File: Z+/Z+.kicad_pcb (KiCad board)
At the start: 4 copper layers, 98 x 98 mm, 159 parts, among them J1 200528-0100, Q1 NX3008NBKS, Q10 NX3008NBKS, Q11 MBT2222ADW1T1, Q12 MBT2222ADW1T1, Q13 NX3008NBKS, Q14 NX3008NBKS, Q15 MBT2222ADW1T1, Q16 MBT2222ADW1T1, Q2 NX3008NBKS, Q3 MBT2222ADW1T1, Q4 MBT2222ADW1T1, Q5 NX3008NBKS, Q6 NX3008NBKS, Q7 MBT2222ADW1T1, Q8 MBT2222ADW1T1, Q9 NX3008NBKS, U1 SI3865DDV-T1-GE3, U2 LTC4376CDHD_PBF, U4 ADM1176-1ARMZ-R7, U5 ADM1176-1ARMZ-R7, U6 NCV891330PD50R2G, U7 DRV8830DRC, U8 LTC3130, U9 SunSensor

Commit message: Z+ updates WIP
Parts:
- removed C34, C35: 0.1uF, Capacitor_SMD:C_0402_1005Metric
- removed FL1: SRF2012, SolarPanels:SRF2012
- removed L2: 6.8uH, Inductor_SMD:L_Coilcraft_LPS4018
- removed Ref**: Val**, custom-footprints:ypanel
- added D10: DFLS130L-7, Diode_SMD:D_PowerDI-123, B.Cu at (18.9, 74.8)
- added F1: Fuse_Small, Fuse:Fuse_0603_1608Metric, B.Cu at (-19.4, 101.4)
- added F2: Fuse_Small, Fuse:Fuse_0603_1608Metric, B.Cu at (-19.4, 103.9)
- added F3: Fuse_Small, Fuse:Fuse_0603_1608Metric, B.Cu at (-19.4, 106.5)
- added F4: Fuse_Small, Fuse:Fuse_0603_1608Metric, B.Cu at (-19.4, 109.0)
- added F5: 500mA, Fuse:Fuse_0603_1608Metric, B.Cu at (80.9, 117.2)
- added F6: 500mA, Fuse:Fuse_0603_1608Metric, B.Cu at (17.9, 87.4)
- added F7: 100mA, Fuse:Fuse_0603_1608Metric, B.Cu at (24.0, 58.5)
- added Q17: MBT2222ADW1T1, Package_TO_SOT_SMD:SOT-363_SC-70-6, B.Cu at (46.8, 56.7)
- added Q18: NX3008NBKS, Package_TO_SOT_SMD:SOT-363_SC-70-6, B.Cu at (46.8, 60.6)
- added Q19: MBT2222ADW1T1, Package_TO_SOT_SMD:SOT-363_SC-70-6, B.Cu at (57.1, 56.7)
- added Q20: NX3008NBKS, Package_TO_SOT_SMD:SOT-363_SC-70-6, B.Cu at (67.3, 76.3)
- added Q21: MBT2222ADW1T1, Package_TO_SOT_SMD:SOT-363_SC-70-6, B.Cu at (57.1, 95.8)
- added Q22: NX3008NBKS, Package_TO_SOT_SMD:SOT-363_SC-70-6, B.Cu at (57.1, 99.8)
- added Q23: MBT2222ADW1T1, Package_TO_SOT_SMD:SOT-363_SC-70-6, B.Cu at (57.1, 103.7)
- added Q24: NX3008NBKS, Package_TO_SOT_SMD:SOT-363_SC-70-6, B.Cu at (77.6, 56.7)
- added Q25: MBT2222ADW1T1, Package_TO_SOT_SMD:SOT-363_SC-70-6, B.Cu at (77.6, 60.6)
- added Q26: NX3008NBKS, Package_TO_SOT_SMD:SOT-363_SC-70-6, B.Cu at (46.8, 76.3)
- added Q27: MBT2222ADW1T1, Package_TO_SOT_SMD:SOT-363_SC-70-6, B.Cu at (46.8, 80.2)
- added R100: DNI (0R), Resistor_SMD:R_0603_1608Metric, B.Cu at (63.2, 63.5)
- added R101: 10K, Resistor_SMD:R_0603_1608Metric, B.Cu at (63.2, 66.0)
- added R102: 10K, Resistor_SMD:R_0603_1608Metric, B.Cu at (63.2, 68.5)
- added R103: 200K, Resistor_SMD:R_0603_1608Metric, B.Cu at (63.2, 71.0)
- added R64: DNI (0R), Resistor_SMD:R_0603_1608Metric, B.Cu at (42.7, 63.5)
- added R65: 10K, Resistor_SMD:R_0603_1608Metric, B.Cu at (42.7, 66.0)
- added R75: 100K, Resistor_SMD:R_0603_1608Metric, B.Cu at (63.2, 80.5)
- added R76: DNI (0R), Resistor_SMD:R_0603_1608Metric, B.Cu at (63.2, 83.0)
- added R77: 10K, Resistor_SMD:R_0603_1608Metric, B.Cu at (63.2, 85.6)
- added R78: 10K, Resistor_SMD:R_0603_1608Metric, B.Cu at (63.2, 88.1)
- added R79: 200K, Resistor_SMD:R_0603_1608Metric, B.Cu at (63.2, 90.6)
- added R80: 680R, Resistor_SMD:R_0603_1608Metric, B.Cu at (52.9, 97.6)
- added R81: 100K, Resistor_SMD:R_0603_1608Metric, B.Cu at (52.9, 100.1)
- added R82: DNI (0R), Resistor_SMD:R_0603_1608Metric, B.Cu at (52.9, 102.6)
- added R83: 10K, Resistor_SMD:R_0603_1608Metric, B.Cu at (52.9, 105.1)
- added R84: 10K, Resistor_SMD:R_0603_1608Metric, B.Cu at (52.9, 107.6)
- added R85: 200K, Resistor_SMD:R_0603_1608Metric, B.Cu at (52.9, 110.1)
- added R86: 680R, Resistor_SMD:R_0603_1608Metric, B.Cu at (73.5, 58.5)
- added R87: 100K, Resistor_SMD:R_0603_1608Metric, B.Cu at (73.5, 61.0)
- added R88: DNI (0R), Resistor_SMD:R_0603_1608Metric, B.Cu at (73.5, 63.5)
- added R89: 10K, Resistor_SMD:R_0603_1608Metric, B.Cu at (73.5, 66.0)
- added R90: 10K, Resistor_SMD:R_0603_1608Metric, B.Cu at (73.5, 68.5)
- added R91: 200K, Resistor_SMD:R_0603_1608Metric, B.Cu at (73.5, 71.0)
- added R92: 680R, Resistor_SMD:R_0603_1608Metric, B.Cu at (42.7, 78.0)
- added R93: 100K, Resistor_SMD:R_0603_1608Metric, B.Cu at (42.7, 80.5)
- added R94: DNI (0R), Resistor_SMD:R_0603_1608Metric, B.Cu at (42.7, 83.0)
- added R95: 10K, Resistor_SMD:R_0603_1608Metric, B.Cu at (42.7, 85.6)
- added R96: 10K, Resistor_SMD:R_0603_1608Metric, B.Cu at (42.7, 88.1)
- added R97: 200K, Resistor_SMD:R_0603_1608Metric, B.Cu at (42.7, 90.6)
- added R98: 680R, Resistor_SMD:R_0603_1608Metric, B.Cu at (63.2, 58.5)
- added R99: 100K, Resistor_SMD:R_0603_1608Metric, B.Cu at (63.2, 61.0)
- added U3: SunSensor, Argus-IC:SunSensor, F.Cu at (103.5, 101.9)
- C1, C2, C5, C6, C7, C8: value 10nF -> 100nF
- C10: value 1nF -> 0.1uF
- C11: value 1uF -> 10uF; footprint Capacitor_SMD:C_1206_3216Metric -> Capacitor_SMD:C_1210_3225Metric
- C12: footprint Capacitor_SMD:C_0402_1005Metric -> Capacitor_SMD:C_0603_1608Metric; moved to B.Cu
- C13: value 3.3nF -> 1nF
- C14: value 3.3nF -> 0.1uF
- C15: value 4.7uF -> 10nF; footprint Capacitor_SMD:C_1210_3225Metric -> Capacitor_SMD:C_0603_1608Metric
- C16: value 0.1uF -> 10nF; footprint Capacitor_SMD:C_0805_2012Metric -> Capacitor_SMD:C_0603_1608Metric
- C17: value 1uF -> 3.3nF; footprint Capacitor_SMD:C_0805_2012Metric -> Capacitor_SMD:C_0603_1608Metric
- C18: value 0.1uF -> 47uF; footprint Capacitor_SMD:C_0603_1608Metric -> Capacitor_SMD:C_1210_3225Metric
- C19: value 0.1uF -> 10uF; footprint Capacitor_SMD:C_0603_1608Metric -> Capacitor_SMD:C_1210_3225Metric
- C20: value 0.1uF -> 1uF; footprint Capacitor_SMD:C_0603_1608Metric -> Capacitor_SMD:C_0805_2012Metric
- C21: value 10uF -> 1uF; footprint Capacitor_SMD:C_1206_3216Metric -> Capacitor_SMD:C_0805_2012Metric
- C22, C23: value 10uF -> 22nF; footprint Capacitor_SMD:C_1206_3216Metric -> Capacitor_SMD:C_0603_1608Metric
- C24: value 47uF -> 4.7uF; footprint Capacitor_SMD:C_1210_3225Metric -> Capacitor_SMD:C_0603_1608Metric
- C25: value 10uF -> 1uF; footprint Capacitor_SMD:C_1210_3225Metric -> Capacitor_SMD:C_0805_2012Metric
- C26: value 1uF -> 47uF; footprint Capacitor_SMD:C_0805_2012Metric -> Capacitor_SMD:C_1210_3225Metric
- C27, C31: value 1uF -> 10nF; footprint Capacitor_SMD:C_0805_2012Metric -> Capacitor_SMD:C_0603_1608Metric
- C28, C29: value 22nF -> 10nF
- C30: value 4.7uF -> 10nF
- C32: value 47uF -> 10nF; footprint Capacitor_SMD:C_1210_3225Metric -> Capacitor_SMD:C_0603_1608Metric
- C33: value 0.1uF -> 10nF; footprint Capacitor_SMD:C_0402_1005Metric -> Capacitor_SMD:C_0603_1608Metric; moved to B.Cu
- C9: value 10uF -> 10nF; footprint Capacitor_SMD:C_1206_3216Metric -> Capacitor_SMD:C_0603_1608Metric
- D1: value DFLS130L-7 -> ESD5Zxx; footprint Diode_SMD:D_PowerDI-123 -> Diode_SMD:D_SOD-523; moved to B.Cu
- D2: value DFLS130L-7 -> PMEG4005EH; footprint Diode_SMD:D_PowerDI-123 -> Diode_SMD:D_SOD-123F; moved to B.Cu
- D3: value DFLS130L-7 -> GREEN; footprint Diode_SMD:D_PowerDI-123 -> LED_SMD:LED_0603_1608Metric; moved to B.Cu
- D4: value DFLS130L-7 -> 10V; footprint Diode_SMD:D_PowerDI-123 -> Diode_SMD:Nexperia_DSN1608-2_1.6x0.8mm; moved to B.Cu
- D5, D6: moved to B.Cu
- D7: value BAS16HT1G -> DFLS130L-7; footprint Diode_SMD:D_SOD-323 -> Diode_SMD:D_PowerDI-123
- D8: value NRVB440MFS -> DFLS130L-7; footprint SolarPanels:NRVB440MFSWFT1G -> Diode_SMD:D_PowerDI-123
- D9: value LSM115 -> DFLS130L-7; footprint SolarPanels:DO-214BA_MCH -> Diode_SMD:D_PowerDI-123
- H1, H2, H3, H4, H5, H6, H7, H8: footprint SolarPanels:MountingHole_3.2mm_M3_DIN965_Pad_TopBottom -> Argus-Miscellaneous:MountingHole_3.2mm_M3_DIN965_Pad_TopBottom
- J1: footprint Connector_FFC-FPC:Molex_200528-0100_1x10-1MP_P1.00mm_Horizontal -> Argus-Connectors:Molex_200528-0100_1x10-1MP_P1.00mm_Horizontal
- L1: value XGL3520-222 -> 6.8uH; footprint SolarPanels:XGL3520 -> Argus-Passives:L_Coilcraft_LPS4018
- Q12, Q16, Q3: value MBT2222ADW1T1 -> NX3008NBKS
- Q13, Q2, Q6: value NX3008NBKS -> MBT2222ADW1T1
- Q7: value MBT2222ADW1T1 -> SiRA99DP; footprint Package_TO_SOT_SMD:SOT-363_SC-70-6 -> Argus-Miscellaneous:PowerPAK SO-8
- Q8: value MBT2222ADW1T1 -> IRLML2803; footprint Package_TO_SOT_SMD:SOT-363_SC-70-6 -> Package_TO_SOT_SMD:SOT-23
- Q9: value NX3008NBKS -> SiRA99DP; footprint Package_TO_SOT_SMD:SOT-363_SC-70-6 -> Argus-Miscellaneous:PowerPAK SO-8
- R1, R68, R74: value 0R -> 680R
- R10, R11: value 680R -> 10K
- R12: value 100K -> 200K
- R13, R7: value 100K -> 680R
- R14: value DNI (0R) -> 100K
- R18, R41, R54: value 10K -> 200K
- R19: value 200K -> 2.7k
- R2: value 0R -> 100K
- R20, R28, R29, R30, R59: value 10K -> 0R
- R21, R31, R57: value 200K -> 0R
- R22: value 680R -> 10k
- R23: value 680R -> 4k7
- R24: value DNI (0R) -> 10k
- R25: value DNI (0R) -> 0R
- R26: value 100K -> 0R
- R27: value 100K -> 10k
- R3, R70: value 0R -> DNI (0R)
- R32: value 10K -> TBD
- R33: value 200K -> 1k
- R34, R35: value DNI (0R) -> TBD
- R37: value 680R -> 100K
- R38: value 100K -> DNI (0R)
- R39: value 100K -> 10K
- R4, R66, R72: value 0R -> 10K
- R42: value 10K -> 680R
- R43: value 200K -> 100K
- R44: value 10K -> DNI (0R)
- R45: value 200K -> 10K
- R46: value DNI (0R) -> 10K
- R47: value DNI (0R) -> 200K
- R48, R49: value 680R -> 1.91M
- R5: value R_Small -> 10K
- R50: value 100K -> 126k
- R51: value 100K -> 182k
- R52, R69: value 10K -> 100K
- R53: value 10K -> 1.47M
- R55: value 200K -> ?R; footprint Resistor_SMD:R_0603_1608Metric -> Resistor_SMD:R_2512_6332Metric
- R56: value 10K -> 1K
- R58: value 100K -> 0R (DNI)
- R6: value R_Small -> 200K
- R60, R61: value ?R -> 0R; footprint Resistor_SMD:R_2512_6332Metric -> Resistor_SMD:R_0603_1608Metric
- R62: value 1K -> 680R
- R63: value 1K -> 100K
- R67, R73: value 0R -> 200K
- R71: value 0R (DNI) -> 10K
- R8: value R_Small -> 100K
- R9: value R_Small -> DNI (0R)
- SC1, SC2, SC3, SC4, SC5, SC6: value SM141K06TF -> SM141K06L; footprint SolarPanels:SM141K06TF -> Argus-Miscellaneous:SM141K06TF
- U1: value SI3865DDV-T1-GE3 -> USBLC6-2P6; footprint Package_TO_SOT_SMD:SOT-23-6 -> Package_TO_SOT_SMD:SOT-666
- U2: value LTC4376CDHD_PBF -> SunSensor; footprint Package_DFN_QFN:DFN-16-1EP_4x5mm_P0.5mm_EP2.44x4.34mm -> Argus-IC:SunSensor
- U4, U5: value ADM1176-1ARMZ-R7 -> SunSensor; footprint Package_SO:MSOP-10_3x3mm_P0.5mm -> Argus-IC:SunSensor
- U6: value NCV891330PD50R2G -> LTC4412xS6; footprint Package_SO:SOIC-8-1EP_3.9x4.9mm_P1.27mm_EP2.514x3.2mm -> Package_TO_SOT_SMD:TSOT-23-6
- U7: value DRV8830DRC -> DRV8235RTER; footprint Package_SON:VSON-10-1EP_3x3mm_P0.5mm_EP1.65x2.4mm -> Argus-IC:WQFN16_RTE_TEX
- U8: value LTC3130 -> ADM1176-1ARMZ-R7; footprint Package_DFN_QFN:QFN-20-1EP_3x4mm_P0.5mm_EP1.65x2.65mm -> Package_SO:MSOP-10_3x3mm_P0.5mm
- U9: value SunSensor -> LTC3130; footprint SolarPanels:SunSensor -> Package_DFN_QFN:QFN-20-1EP_3x4mm_P0.5mm_EP1.65x2.65mm; moved to B.Cu
- moved C7 183.6 mm to (-19.4, 96.4), turned to 180 degrees
- moved U2 182.3 mm to (-8.12, 92.1), turned to 180 degrees
- moved U4 179.0 mm to (-8.12, 100.1)
- moved D3 177.8 mm to (18.0, 97.5), turned to 180 degrees
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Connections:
- C1 pad 1: Net-(Q1B-G1) -> MAIN_3V3
- C10 pad 1: Net-(U1-R1,C1) -> Net-(D2-A)
- C10 pad 2: Net-(D9-A) -> GND
- C11 pad 1: Net-(D9-A) -> /Coil Driver/VM
- C12 pad 1: 3.3V -> /Coil Driver/VM
- C13 pad 1: GND -> /Coil Driver/IPROPI
- C13 pad 2: Net-(U4-TIMER) -> GND
- C14 pad 1: GND -> /Coil Driver/VREF
- C14 pad 2: Net-(U5-TIMER) -> GND
- C15 pad 1: GND -> Net-(Q10B-G1)
- C15 pad 2: VDRIVE -> GND
- C16 pad 1: +5V -> Net-(Q12B-G1)
- C17 pad 2: VDRIVE -> Net-(U8-TIMER)
- C18 pad 1: GND -> /Solar Charger/MPPT2/VIN
- C18 pad 2: Net-(D7-A) -> GND
- C19 pad 1: Net-(D7-K) -> /Solar Charger/MPPT2/VIN
- C19 pad 2: Net-(D8-K) -> GND
- C2 pad 1: Net-(Q2B-G1) -> PERI_3V3
- C20 pad 1: GND -> /Solar Charger/MPPT2/VIN
- C20 pad 2: +5V -> GND
- C21 pad 1: GND -> /Solar Charger/MPPT2/VIN
- C21 pad 2: +5V -> GND
- C22 pad 1: GND -> Net-(U9-SW1)
- C22 pad 2: +5V -> Net-(U9-BST1)
- C23 pad 1: GND -> Net-(U9-BST2)
- C23 pad 2: +5V -> Net-(U9-SW2)
- C24 pad 1: VSOLAR -> /Solar Charger/MPPT2/VCC
- C25 pad 1: VSOLAR -> /Solar Charger/Charge OR-ing2/IN
- C26 pad 1: VSOLAR -> /Solar Charger/Charge OR-ing2/IN
- C27 pad 1: VSOLAR -> Net-(Q14B-G1)
- C28 pad 1: Net-(U8-SW1) -> Net-(Q16B-G1)
- C28 pad 2: Net-(U8-BST1) -> GND
- C29 pad 1: Net-(U8-BST2) -> Net-(Q18B-G1)
- C29 pad 2: Net-(U8-SW2) -> GND
- C3 pad 1: Net-(Q5B-G1) -> Net-(Q1B-G1)
- C30 pad 1: /MPPT/VCC -> Net-(Q20B-G1)
- C31 pad 1: /Charge OR-ing/IN -> Net-(Q22B-G1)
- C32 pad 1: /Charge OR-ing/IN -> Net-(Q24B-G1)
- C33 pad 1: 3.3V -> Net-(Q26B-G1)
- C4 pad 1: Net-(Q6B-G1) -> Net-(Q3B-G1)
- C5 pad 1: Net-(Q9B-G1) -> /Sun Pyramid/LS1_3V3
- C6 pad 1: Net-(Q10B-G1) -> /Sun Pyramid/LS2_3V3
- C7 pad 1: Net-(Q13B-G1) -> /Sun Pyramid/LS3_3V3
- C8 pad 1: Net-(Q14B-G1) -> /Sun Pyramid/LS0_3V3
- C9 pad 1: /Charge OR-ing/IN -> Net-(Q5B-G1)
- D1 pad 1: Net-(D1-K) -> PERI_3V3
- D2 pad 1: Net-(D2-K) -> VCHRG
- D2 pad 2: Net-(D1-K) -> Net-(D2-A)
- D3 pad 1: Net-(D3-K) -> GND
- D3 pad 2: Net-(D2-K) -> Net-(D3-A)
- D4 pad 1: Net-(D4-K) -> /Coil Driver/VM
- D4 pad 2: Net-(D3-K) -> GND
- D5 pad 2: Net-(D4-K) -> GND
- D6 pad 1: VSOLAR -> Net-(D6-K)
- D7 pad 2: Net-(D7-A) -> Net-(D6-K)
- D8 pad 2: GND -> Net-(D7-K)
- D9 pad 1: VCHRG -> Net-(D10-A)
- D9 pad 2: Net-(D9-A) -> Net-(D8-K)
- J1 pad 1: SCL -> Net-(J1-Pin_1)
- J1 pad 2: SDA -> Net-(J1-Pin_2)
- J1 pad 3: 3.3V -> COIL_DRIVER_EN
- J1 pad 4: 3.3V -> MAIN_3V3
- J1 pad 5: GND -> PERI_3V3
- L1 pad 1: Net-(D8-K) -> Net-(U9-SW1)
- L1 pad 2: +5V -> Net-(U9-SW2)
- Q11 pad 4: SCL_SPWR -> /Coil Driver/SCL_M
- Q11 pad 5: Net-(Q11B-B2) -> Net-(Q10A-D1)
- Q11 pad 6: SCL_SPWR -> /Coil Driver/SCL_M
- Q12 pad 1: SCL -> GND
- Q12 pad 2: Net-(Q12A-B1) -> Net-(Q12A-G2)
- Q12 pad 3: SCL -> Net-(Q12A-G2)
- Q12 pad 4: SCL_CPWR -> GND
- Q12 pad 5: Net-(Q10A-D1) -> Net-(Q12B-G1)
- Q12 pad 6: SCL_CPWR -> Net-(Q12A-D1)
- Q13 pad 1: GND -> SDA
- Q13 pad 2: Net-(Q13A-G2) -> Net-(Q13A-B1)
- Q13 pad 3: Net-(Q13A-G2) -> SDA
- Q13 pad 4: GND -> /Coil Driver/SDA_M
- Q13 pad 5: Net-(Q13B-G1) -> Net-(Q12A-D1)
- Q13 pad 6: Net-(Q13A-D1) -> /Coil Driver/SDA_M
- Q15 pad 5: Net-(Q13A-D1) -> Net-(Q14A-D1)
- Q16 pad 1: SDA -> GND
- Q16 pad 2: Net-(Q16A-B1) -> Net-(Q16A-G2)
- Q16 pad 3: SDA -> Net-(Q16A-G2)
- Q16 pad 4: SDA_CPWR -> GND
- Q16 pad 5: Net-(Q14A-D1) -> Net-(Q16B-G1)
- Q16 pad 6: SDA_CPWR -> Net-(Q16A-D1)
- Q2 pad 1: GND -> SCL
- Q2 pad 2: Net-(Q2A-G2) -> Net-(Q2A-B1)
- Q2 pad 3: Net-(Q2A-G2) -> SCL
- Q2 pad 4: GND -> /Sun Pyramid/LS0_SCL
- Q2 pad 5: Net-(Q2B-G1) -> Net-(Q1A-D1)
- Q2 pad 6: Net-(Q2A-D1) -> /Sun Pyramid/LS0_SCL
- Q3 pad 1: SCL -> GND
- Q3 pad 2: Net-(Q3A-B1) -> Net-(Q3A-G2)
- Q3 pad 3: SCL -> Net-(Q3A-G2)
- Q3 pad 4: SCL_LS -> GND
- Q3 pad 5: Net-(Q1A-D1) -> Net-(Q3B-G1)
- Q3 pad 6: SCL_LS -> Net-(Q3A-D1)
- Q4 pad 1: SCL -> SDA
- Q4 pad 3: SCL -> SDA
- Q4 pad 4: SCL_M -> /Sun Pyramid/LS0_SDA
- Q4 pad 5: Net-(Q2A-D1) -> Net-(Q3A-D1)
- Q4 pad 6: SCL_M -> /Sun Pyramid/LS0_SDA
- Q6 pad 1: GND -> SCL
- Q6 pad 2: Net-(Q6A-G2) -> Net-(Q6A-B1)
- Q6 pad 3: Net-(Q6A-G2) -> SCL
- Q6 pad 4: GND -> /Sun Pyramid/LS1_SCL
- Q6 pad 5: Net-(Q6B-G1) -> Net-(Q5A-D1)
- Q6 pad 6: Net-(Q6A-D1) -> /Sun Pyramid/LS1_SCL
- Q7 pad 1: SDA -> Net-(Q7-G)
- Q7 pad 2: Net-(Q7A-B1) -> VCHRG
- Q7 pad 3: SDA -> Net-(D2-A)
- Q8 pad 1: SDA -> Net-(Q8-G)
- Q8 pad 2: Net-(Q8A-B1) -> GND
- Q8 pad 3: SDA -> Net-(Q8-D)
- Q9 pad 1: GND -> Net-(Q8-D)
- Q9 pad 2: Net-(Q9A-G2) -> /Coil Driver/VM
- Q9 pad 3: Net-(Q9A-G2) -> Net-(Q9-S)
- R1 pad 1: COIL_P -> Net-(Q2A-B1)
- R1 pad 2: /coil -> Net-(Q1A-D1)
- R10 pad 1: Net-(Q3A-B1) -> /Sun Pyramid/LS0_3V3
- R10 pad 2: Net-(Q1A-D1) -> Net-(Q3A-D1)
- R11 pad 1: Net-(Q4A-B1) -> /Sun Pyramid/LS0_3V3
- R11 pad 2: Net-(Q2A-D1) -> /Sun Pyramid/LS0_SDA
- R12 pad 1: 3.3V -> /Sun Pyramid/LS0_SDA
- R12 pad 2: Net-(Q1A-G2) -> Net-(Q3B-G1)
- R13 pad 1: 3.3V -> Net-(Q6A-B1)
- R13 pad 2: Net-(Q2A-G2) -> Net-(Q5A-D1)
- R14 pad 1: SCL_LS -> /Sun Pyramid/LS1_3V3
- R14 pad 2: SCL -> Net-(Q5A-G2)
- R15 pad 1: SDA_LS -> /Sun Pyramid/LS1_SCL
- R15 pad 2: SDA -> SCL
- R16 pad 1: 3.3V -> /Sun Pyramid/LS1_3V3
- R16 pad 2: Net-(Q1A-D1) -> Net-(Q5A-D1)
- R17 pad 1: 3.3V -> /Sun Pyramid/LS1_3V3
- R17 pad 2: Net-(Q2A-D1) -> /Sun Pyramid/LS1_SCL
- R18 pad 1: 3.3V -> /Sun Pyramid/LS1_SCL
- R18 pad 2: SCL_LS -> Net-(Q5B-G1)
- R19 pad 1: SCL_LS -> COIL_DRIVER_EN
- R19 pad 2: Net-(Q1B-G1) -> Net-(D3-A)
- R2 pad 1: /coil -> /Sun Pyramid/LS0_3V3
- R2 pad 2: COIL_P -> Net-(Q1A-G2)
- R20 pad 1: 3.3V -> COIL_P
- R20 pad 2: SCL_M -> /Coil Driver/coil
- R21 pad 1: SCL_M -> /Coil Driver/coil
- R21 pad 2: Net-(Q2B-G1) -> COIL_P
- R22 pad 1: Net-(Q7A-B1) -> GND
- R22 pad 2: Net-(Q5A-D1) -> COIL_DRIVER_EN
- R23 pad 1: Net-(Q8A-B1) -> COIL_DRIVER_EN
- R23 pad 2: Net-(Q6A-D1) -> Net-(Q8-G)
- R24 pad 1: SCL_SPWR -> Net-(Q8-D)
- R24 pad 2: SCL -> Net-(Q9-S)
- R25 pad 1: SDA_SPWR -> COIL_N
- R25 pad 2: SDA -> /Coil Driver/coil
- R26 pad 1: 3.3V -> /Coil Driver/coil
- R26 pad 2: Net-(Q5A-G2) -> COIL_N
- R27 pad 1: 3.3V -> MAIN_3V3
- R27 pad 2: Net-(Q6A-G2) -> Net-(U7-NFAULT)
- R28 pad 1: 3.3V -> /Coil Driver/A0_COIL
- R28 pad 2: Net-(Q5A-D1) -> MAIN_3V3
- R29 pad 1: 3.3V -> GND
- R29 pad 2: Net-(Q6A-D1) -> /Coil Driver/A0_COIL
- R3 pad 1: COIL_N -> /Sun Pyramid/LS0_SCL
- R3 pad 2: /coil -> SCL
- R30 pad 1: 3.3V -> /Coil Driver/A1_COIL
- R30 pad 2: SDA_LS -> MAIN_3V3
- R31 pad 1: SDA_LS -> GND
- R31 pad 2: Net-(Q5B-G1) -> /Coil Driver/A1_COIL
- R32 pad 1: 3.3V -> /Coil Driver/IPROPI
- R32 pad 2: SDA_M -> GND
- R33 pad 1: SDA_M -> Net-(U7-NSLEEP)
- R33 pad 2: Net-(Q6B-G1) -> PERI_3V3
- R34 pad 1: SCL_M -> MAIN_3V3
- R34 pad 2: SCL -> /Coil Driver/VREF
- R35 pad 1: SDA_M -> /Coil Driver/VREF
- R35 pad 2: SDA -> GND
- R36 pad 2: Net-(Q11B-B2) -> Net-(Q10A-D1)
- R37 pad 1: Net-(Q12A-B1) -> MAIN_3V3
- R37 pad 2: Net-(Q10A-D1) -> Net-(Q10A-G2)
- R38 pad 1: 3.3V -> /Coil Driver/SCL_M
- R38 pad 2: Net-(Q9A-G2) -> SCL
- R39 pad 1: 3.3V -> MAIN_3V3
- R39 pad 2: Net-(Q10A-G2) -> Net-(Q10A-D1)
- R4 pad 1: /coil -> /Sun Pyramid/LS0_3V3
- R4 pad 2: COIL_N -> Net-(Q1A-D1)
- R40 pad 1: 3.3V -> MAIN_3V3
- R40 pad 2: Net-(Q11B-B2) -> /Coil Driver/SCL_M
- R41 pad 1: 3.3V -> /Coil Driver/SCL_M
- R41 pad 2: Net-(Q10A-D1) -> Net-(Q10B-G1)
- R42 pad 1: 3.3V -> Net-(Q13A-B1)
- R42 pad 2: SCL_SPWR -> Net-(Q12A-D1)
- R43 pad 1: SCL_SPWR -> MAIN_3V3
- R43 pad 2: Net-(Q9B-G1) -> Net-(Q12A-G2)
- R44 pad 1: 3.3V -> /Coil Driver/SDA_M
- R44 pad 2: SCL_CPWR -> SDA
- R45 pad 1: SCL_CPWR -> MAIN_3V3
- R45 pad 2: Net-(Q10B-G1) -> Net-(Q12A-D1)
- R46 pad 1: SCL_CPWR -> MAIN_3V3
- R46 pad 2: SCL -> /Coil Driver/SDA_M
- R47 pad 1: SDA_CPWR -> /Coil Driver/SDA_M
- R47 pad 2: SDA -> Net-(Q12B-G1)
- R48 pad 1: Net-(Q15A-B1) -> /Solar Charger/MPPT2/VIN
- R48 pad 2: Net-(Q13A-D1) -> /Solar Charger/MPPT2/RUN
- R49 pad 1: Net-(Q16A-B1) -> /Solar Charger/MPPT2/VIN
- R49 pad 2: Net-(Q14A-D1) -> /Solar Charger/MPPT2/MPPC
- R5 pad 1: VSOLAR -> /Sun Pyramid/LS0_3V3
- R5 pad 2: /MPPT/MPPC -> /Sun Pyramid/LS0_SCL
- R50 pad 1: 3.3V -> /Solar Charger/MPPT2/MPPC
- R50 pad 2: Net-(Q13A-G2) -> GND
- R51 pad 1: 3.3V -> /Solar Charger/MPPT2/RUN
- R51 pad 2: Net-(Q14A-G2) -> GND
- R52 pad 1: 3.3V -> /Solar Charger/PGOOD3
- R52 pad 2: Net-(Q13A-D1) -> /Solar Charger/Charge OR-ing2/IN
- R53 pad 1: 3.3V -> /Solar Charger/Charge OR-ing2/IN
- R53 pad 2: Net-(Q14A-D1) -> /Solar Charger/MPPT2/FB
- R54 pad 1: 3.3V -> /Solar Charger/MPPT2/FB
- R54 pad 2: SDA_SPWR -> GND
- R55 pad 1: SDA_SPWR -> VCHRG
- R55 pad 2: Net-(Q13B-G1) -> VBATT
- R56 pad 1: 3.3V -> VCHRG
- R56 pad 2: SDA_CPWR -> Net-(U8-ON)
- R57 pad 1: SDA_CPWR -> GND
- R57 pad 2: Net-(Q14B-G1) -> Net-(U8-A0)
- R58 pad 1: Net-(U1-R1,C1) -> Net-(U9-ILIM)
- R58 pad 2: /Charge OR-ing/IN -> /Solar Charger/MPPT2/VCC
- R59 pad 1: Net-(U1-R2) -> Net-(U9-ILIM)
- R6 pad 1: /MPPT/MPPC -> /Sun Pyramid/LS0_SCL
- R6 pad 2: GND -> Net-(Q1B-G1)
- R60 pad 1: VCHRG -> Net-(U9-MODE)
- R60 pad 2: VBATT -> GND
- R61 pad 1: VDRIVE -> GND
- R61 pad 2: VBATT -> Net-(U9-EXTVCC)
- R62 pad 1: VCHRG -> Net-(Q15A-B1)
- R62 pad 2: Net-(U4-ON) -> Net-(Q14A-D1)
- R63 pad 1: VDRIVE -> MAIN_3V3
- R63 pad 2: Net-(U5-ON) -> Net-(Q14A-G2)
- R66 pad 1: GND -> MAIN_3V3
- R66 pad 2: Net-(U4-A0) -> SDA_SPWR
- R67 pad 1: GND -> SDA_SPWR
- R67 pad 2: Net-(U5-A0) -> Net-(Q14B-G1)
- R68 pad 1: GND -> Net-(Q17A-B1)
- R68 pad 2: Net-(U7-A0) -> Net-(Q16A-D1)
- R69 pad 1: M_FAULT -> MAIN_3V3
- R69 pad 2: VDRIVE -> Net-(Q16A-G2)
- R7 pad 1: /PGOOD1 -> Net-(Q4A-B1)
- R7 pad 2: /Charge OR-ing/IN -> Net-(Q3A-D1)
- R70 pad 1: GND -> SCL_SPWR
- R70 pad 2: Net-(U7-ISENSE) -> SCL
- R71 pad 1: Net-(U8-ILIM) -> MAIN_3V3
- R71 pad 2: /MPPT/VCC -> Net-(Q16A-D1)
- R72 pad 1: Net-(U8-ILIM) -> MAIN_3V3
- R72 pad 2: GND -> SCL_SPWR
- R73 pad 1: Net-(U8-MODE) -> SCL_SPWR
- R73 pad 2: GND -> Net-(Q16B-G1)
- R74 pad 1: GND -> Net-(Q19A-B1)
- R74 pad 2: Net-(U8-EXTVCC) -> Net-(Q18A-D1)
- R8 pad 1: /Charge OR-ing/IN -> /Sun Pyramid/LS0_3V3
- R8 pad 2: /MPPT/FB -> Net-(Q3A-G2)
- R9 pad 1: /MPPT/FB -> /Sun Pyramid/LS0_SDA
- R9 pad 2: GND -> SDA
- SC1 pad 1: Net-(D1-K) -> Net-(D5-K)
- SC2 pad 1: Net-(D2-K) -> Net-(D6-K)
- SC2 pad 2: Net-(D1-K) -> Net-(D5-K)
- SC3 pad 1: Net-(D3-K) -> Net-(D7-K)
- SC3 pad 2: Net-(D2-K) -> Net-(D6-K)
- SC4 pad 1: Net-(D4-K) -> Net-(D8-K)
- SC4 pad 2: Net-(D3-K) -> Net-(D7-K)
- SC5 pad 1: Net-(D5-K) -> Net-(D10-A)
- SC5 pad 2: Net-(D4-K) -> Net-(D8-K)
- SC6 pad 2: Net-(D5-K) -> Net-(D10-A)
- U1 pad 1: Net-(U1-R2) -> Net-(J1-Pin_1)
- U1 pad 2: Net-(D9-A) -> GND
- U1 pad 3: Net-(D9-A) -> Net-(J1-Pin_2)
- U1 pad 4: /Charge OR-ing/IN -> SDA
- U1 pad 5: /PGOOD1 -> MAIN_3V3
- U1 pad 6: Net-(U1-R1,C1) -> SCL
- U2 pad 1: /Charge OR-ing/IN -> /Sun Pyramid/LS0_3V3
- U2 pad 2: /Charge OR-ing/IN -> GND
- U2 pad 3: /Charge OR-ing/IN -> /Sun Pyramid/LS0_ADDR
- U2 pad 4: /Charge OR-ing/IN -> /Sun Pyramid/LS0_SCL
- U2 pad 5: (no net) -> /Sun Pyramid/LS0_SDA
- U4 pad 1: VBATT -> /Sun Pyramid/LS2_3V3
- U4 pad 2: VCHRG -> GND
- U4 pad 3: Net-(U4-ON) -> /Sun Pyramid/LS2_ADDR
- U4 pad 4: GND -> /Sun Pyramid/LS2_SCL
- U4 pad 5: Net-(U4-TIMER) -> /Sun Pyramid/LS2_SDA
- U5 pad 1: VBATT -> /Sun Pyramid/LS3_3V3
- U5 pad 2: VDRIVE -> GND
- U5 pad 3: Net-(U5-ON) -> /Sun Pyramid/LS3_ADDR
- U5 pad 4: GND -> /Sun Pyramid/LS3_SCL
- U5 pad 5: Net-(U5-TIMER) -> /Sun Pyramid/LS3_SDA
- U6 pad 1: VDRIVE -> Net-(D2-A)
- U6 pad 2: Net-(D7-A) -> GND
- U6 pad 3: unconnected-(U6-RSTB-Pad3) -> GND
- U6 pad 4: GND -> unconnected-(U6-STAT-Pad4)
- U6 pad 5: M_FAULT -> Net-(Q7-G)
- U6 pad 6: +5V -> VCHRG
- U7 pad 1: Net-(U7-OUT2) -> /Coil Driver/IPROPI
- U7 pad 10: SCL_M -> /Coil Driver/A0_COIL
- U7 pad 11: GND -> Net-(U7-NSLEEP)
- U7 pad 2: Net-(U7-ISENSE) -> unconnected-(U7-RSVD-Pad2)
- U7 pad 3: Net-(U7-OUT1) -> unconnected-(U7-RSVD-Pad3)
- U7 pad 4: +5V -> Net-(U7-NFAULT)
- U7 pad 5: GND -> /Coil Driver/VM
- U7 pad 6: M_FAULT -> COIL_P
- U7 pad 7: Net-(U7-A0) -> GND
- U7 pad 8: unconnected-(U7-A1-Pad8) -> COIL_N
- U7 pad 9: SDA_M -> /Coil Driver/A1_COIL
- U8 pad 1: Net-(U8-BST1) -> VBATT
- U8 pad 10: Net-(U8-ILIM) -> unconnected-(U8-GATE-Pad10)
- U8 pad 2: VSOLAR -> VCHRG
- U8 pad 3: VSOLAR -> Net-(U8-ON)
- U8 pad 4: VSOLAR -> GND
- U8 pad 5: /MPPT/VCC -> Net-(U8-TIMER)
- U8 pad 6: /MPPT/MPPC -> SCL_SPWR
- U8 pad 7: GND -> SDA_SPWR
- U8 pad 8: GND -> Net-(U8-A0)
- U8 pad 9: /MPPT/FB -> unconnected-(U8-A1-Pad9)
- U9 pad 1: 3.3V -> Net-(U9-BST1)
- U9 pad 10: GND -> Net-(U9-ILIM)
- U9 pad 11: SCL_LS -> Net-(U9-MODE)
- U9 pad 12: SDA_LS -> Net-(U9-EXTVCC)
- U9 pad 13: 3.3V -> /Solar Charger/PGOOD3
- U9 pad 14: GND -> /Solar Charger/Charge OR-ing2/IN
- U9 pad 15: SCL_LS -> Net-(U9-SW2)
- U9 pad 16: SDA_LS -> Net-(U9-BST2)
- U9 pad 2: GND -> /Solar Charger/MPPT2/VIN
- U9 pad 3: SCL_LS -> /Solar Charger/MPPT2/VIN
- U9 pad 4: SDA_LS -> /Solar Charger/MPPT2/RUN
- U9 pad 5: 3.3V -> /Solar Charger/MPPT2/VCC
- U9 pad 6: GND -> /Solar Charger/MPPT2/MPPC
- U9 pad 7: SCL_LS -> GND
- U9 pad 8: SDA_LS -> GND
- U9 pad 9: 3.3V -> /Solar Charger/MPPT2/FB
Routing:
- net /coil: track 23919.4 -> 0.00 mm, vias 3 -> 0
- net (no net): track 0.00 -> 23914.1 mm, vias 0 -> 1
- net Net-(D3-K): track 122.5 -> 0.00 mm
- net SDA: track 99.5 -> 0.00 mm, vias 5 -> 0
- net SCL: track 98.1 -> 0.00 mm, vias 5 -> 0
- net Net-(D2-K): track 77.0 -> 0.00 mm
- net SCL_LS: track 68.0 -> 0.00 mm, vias 2 -> 0
- net SDA_LS: track 67.8 -> 0.00 mm, vias 2 -> 0
- net Net-(D4-K): track 66.7 -> 0.00 mm
- net Net-(D5-K): track 61.0 -> 0.00 mm
- net 3.3V: track 57.6 -> 0.00 mm, vias 27 -> 0
- net VSOLAR: track 54.5 -> 0.00 mm, vias 4 -> 0
- net Net-(D1-K): track 45.4 -> 0.00 mm
- net SDA_M: track 30.1 -> 0.00 mm, vias 2 -> 0
- net SCL_M: track 25.4 -> 0.00 mm, vias 2 -> 0
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- added copper zone on In1.Cu, net COIL_DRIVER_EN
- removed copper zone on B.Cu, net +5V
- removed copper zone on B.Cu, net /Charge OR-ing/IN
- removed copper zone on B.Cu, net /MPPT/VCC
- removed copper zone on B.Cu, net 3.3V
- removed copper zone on In1.Cu, net 3.3V
- removed copper zone on B.Cu, net Net-(D8-K)
- removed copper zone on B.Cu, net Net-(D9-A)
- removed copper zone on B.Cu, net Net-(U8-BST1)
- removed copper zone on B.Cu, net Net-(U8-BST2)
- removed copper zone on B.Cu, net Net-(U8-EXTVCC)
- removed copper zone on B.Cu, net Net-(U8-SW1)
- removed copper zone on B.Cu, net Net-(U8-SW2)
- removed copper zone on B.Cu, net VBATT
- removed copper zone on B.Cu, net VCHRG
- removed copper zone on B.Cu, net VDRIVE
- removed copper zone on B.Cu, net VSOLAR

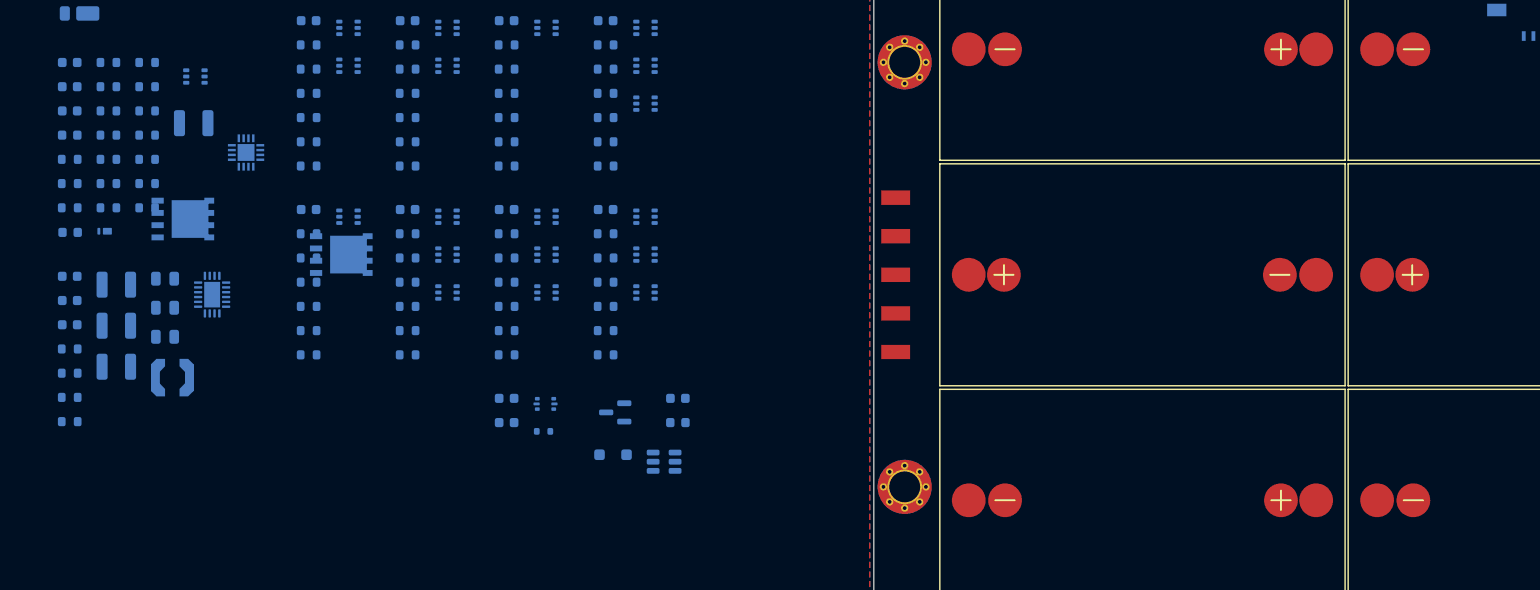
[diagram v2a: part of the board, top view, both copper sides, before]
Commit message: Started layout of coil driver
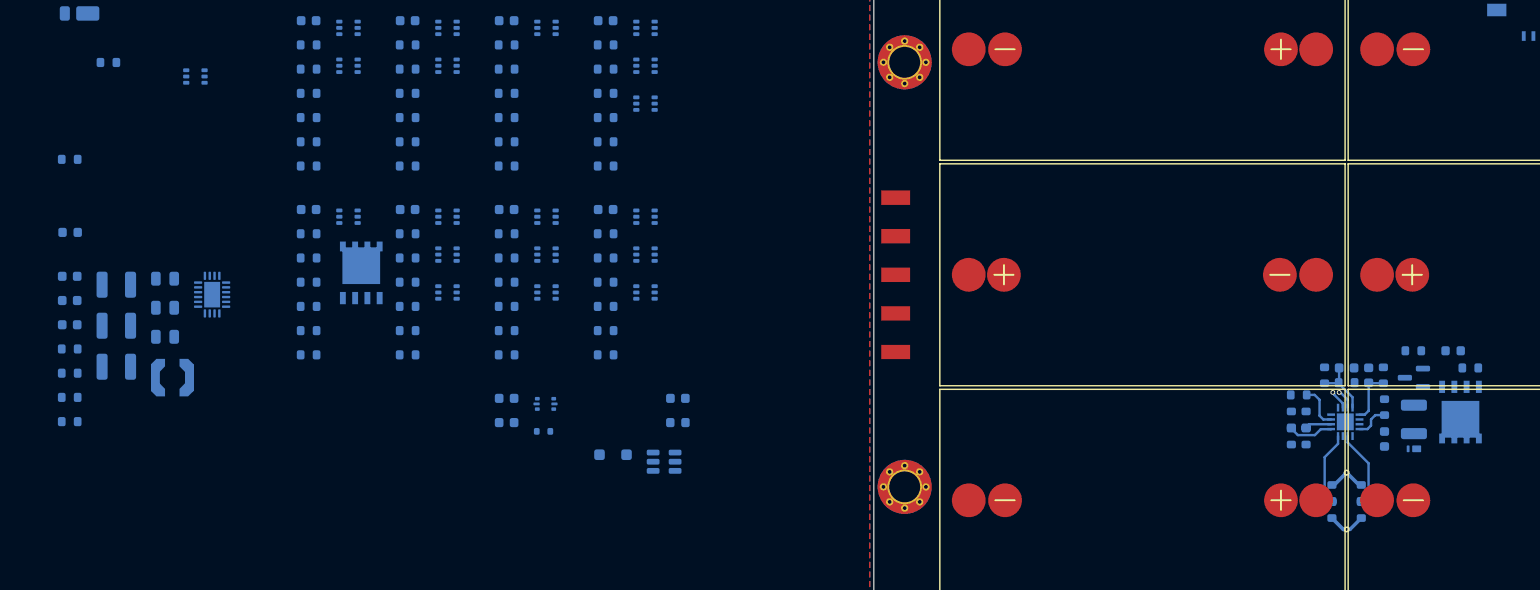
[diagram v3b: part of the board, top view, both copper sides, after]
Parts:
- moved F6 145.1 mm to (161.3, 109.7)
- moved R24 143.6 mm to (163.1, 111.5)
- moved C12 141.7 mm to (154.2, 118.9), turned to 90 degrees
- moved R20 138.1 mm to (151.8, 126.2), turned to -90 degrees
- moved R23 138.0 mm to (157.2, 109.7)
- moved C13 137.9 mm to (152.5, 112.3), turned to 90 degrees
- moved D4 137.5 mm to (157.2, 119.9)
- moved R21 137.1 mm to (151.8, 124.5), turned to -90 degrees
- moved C14 135.0 mm to (150.3, 111.5), turned to 0 degrees
- moved R27 134.3 mm to (154.2, 115.6), turned to -90 degrees
- moved Q9 133.3 mm to (162.1, 116.8), turned to 90 degrees
- moved R25 132.6 mm to (148.7, 126.2), turned to -90 degrees
- moved R26 131.4 mm to (148.7, 124.5), turned to -90 degrees
- moved R32 130.5 mm to (154.1, 112.3), turned to 90 degrees
- moved C11 130.1 mm to (157.2, 116.8), turned to 90 degrees
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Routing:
- net /Coil Driver/coil: track 0.00 -> 23922.6 mm, vias 0 -> 3
- net (no net): track 23914.1 -> 0.00 mm, vias 1 -> 0
- net COIL_P: track 0.00 -> 7.92 mm
- net COIL_N: track 0.00 -> 7.60 mm
- net /Coil Driver/VREF: track 0.00 -> 6.22 mm
- net /Coil Driver/IPROPI: track 0.00 -> 5.56 mm
- net /Coil Driver/A1_COIL: track 0.00 -> 4.65 mm
- net Net-(U7-NSLEEP): track 0.00 -> 4.55 mm
- net Net-(U7-NFAULT): track 0.00 -> 3.56 mm
- net /Coil Driver/A0_COIL: track 0.00 -> 2.72 mm
- net /Coil Driver/SCL_M: track 0.00 -> 2.02 mm, vias 0 -> 1
- net /Coil Driver/SDA_M: track 0.00 -> 2.01 mm, vias 0 -> 1

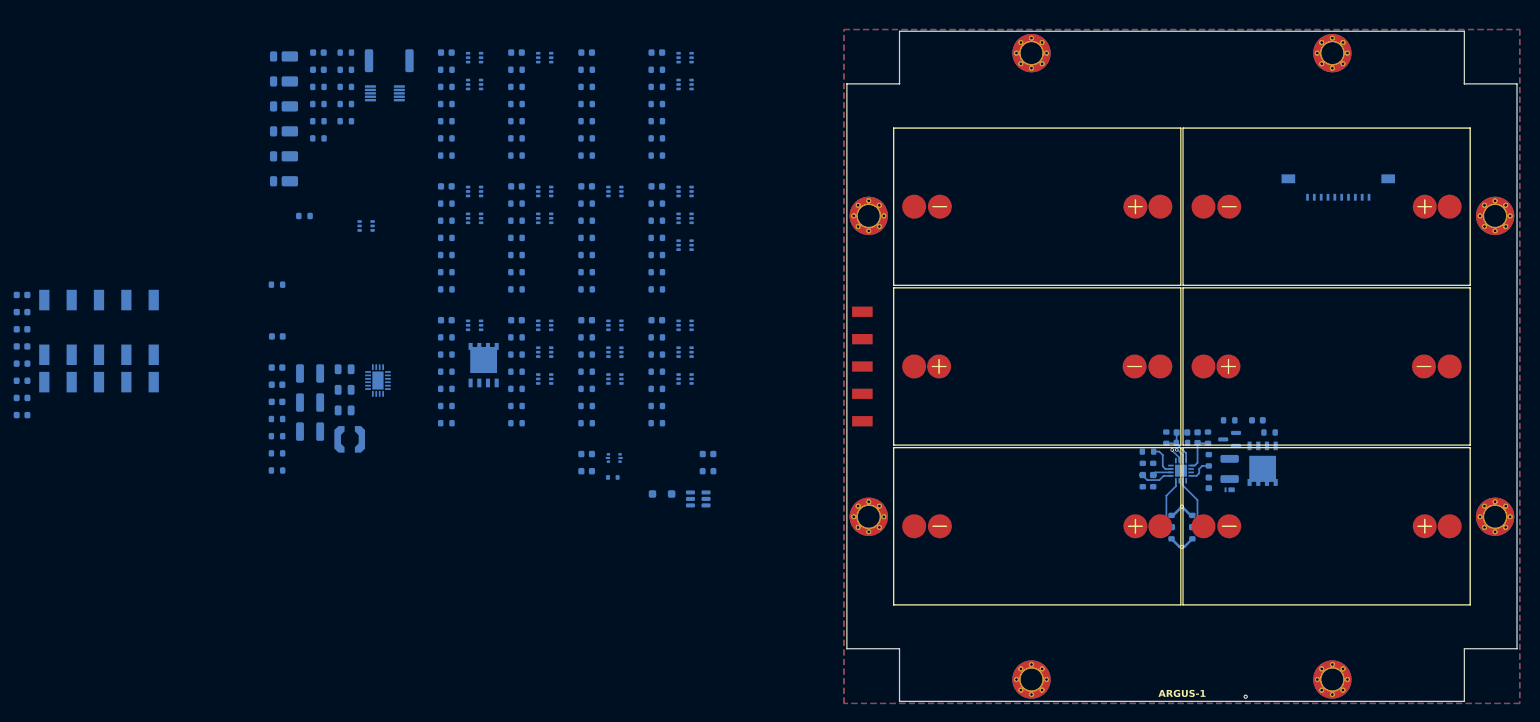
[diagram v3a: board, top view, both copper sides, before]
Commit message: Placed all components
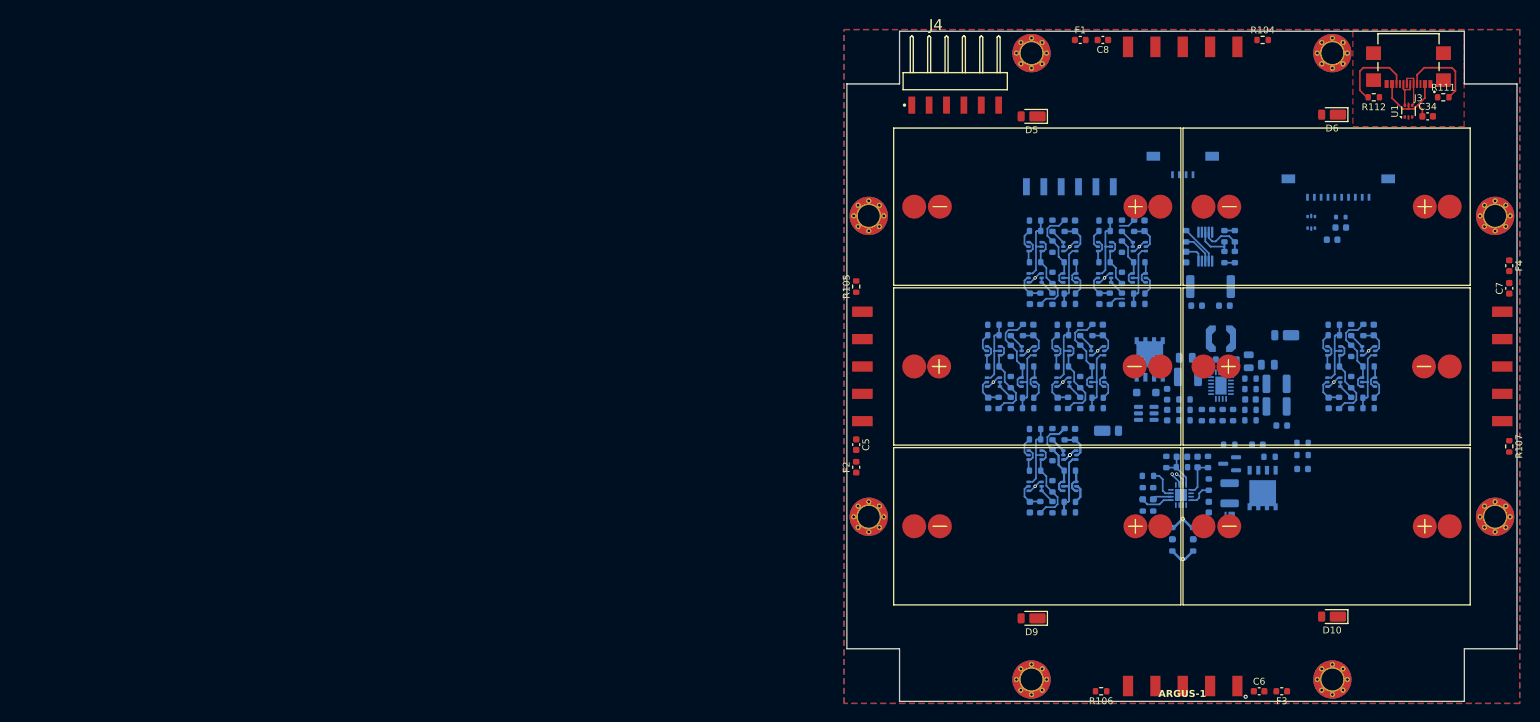
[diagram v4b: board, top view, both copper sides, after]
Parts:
- added C34: 4u7, Capacitor_SMD:C_0603_1608Metric, F.Cu at (186.2, 65.3)
- added F8: 100mA, Fuse:Fuse_0603_1608Metric, B.Cu at (156.5, 93.0)
- added F9: 100mA, Fuse:Fuse_0603_1608Metric, B.Cu at (152.4, 93.0)
- added J2: Conn_01x04_MountingPin, Argus-Connectors:Molex_200528-0040_1x04-1MP_P1.00mm_Horizontal, B.Cu at (150.4, 72.9)
- added J3: USB4110GFA, Argus-Connectors:GCT_USB4110GFA, F.Cu at (183.4, 59.5)
- added J4: BG301-06-X-XXXX-X-X_REVC, Argus-Connectors:GCT_BG301-06-X-XXXX-X-X_REVC, F.Cu at (117.1, 63.6)
- added J5: BG301-06-X-XXXX-X-X_REVC, Argus-Connectors:GCT_BG301-06-X-XXXX-X-X_REVC, B.Cu at (133.9, 75.6)
- added R104: 0R, Resistor_SMD:R_0603_1608Metric, F.Cu at (162.1, 54.1)
- added R105: 0R, Resistor_SMD:R_0603_1608Metric, F.Cu at (102.6, 90.2)
- added R106: 0R, Resistor_SMD:R_0603_1608Metric, F.Cu at (138.4, 149.4)
- added R107: 0R, Resistor_SMD:R_0603_1608Metric, F.Cu at (198.1, 113.5)
- added R108: 0R, Resistor_SMD:R_0603_1608Metric, B.Cu at (156.5, 85.9)
- added R109: 0R, Resistor_SMD:R_0603_1608Metric, B.Cu at (158.0, 82.8)
- added R110: 0R, Resistor_SMD:R_0603_1608Metric, B.Cu at (158.0, 85.9)
- added R111: 5k1, Resistor_SMD:R_0603_1608Metric, F.Cu at (188.5, 62.5)
- added R112: 5k1, Resistor_SMD:R_0603_1608Metric, F.Cu at (178.3, 62.5)
- added U10: USBLC6-2P6, Package_TO_SOT_SMD:SOT-666, B.Cu at (169.2, 80.8)
- C5, C6, C7, C8, D10, D5, D6, D9, F1, F2, F3, F4, U1, U2, U4, U5: moved to F.Cu
- SC1, SC2, SC3, SC4, SC5, SC6: value SM141K06L -> SM141K06TF
- moved F4 218.6 mm to (198.1, 87.1), turned to -90 degrees
- moved C7 217.6 mm to (198.1, 90.4), turned to 90 degrees
- moved U5 205.2 mm to (197.1, 101.9), turned to -90 degrees
- moved C6 189.2 mm to (161.5, 149.4), turned to 0 degrees
- moved F3 189.1 mm to (164.8, 149.4)
- moved D10 166.0 mm to (172.2, 138.4)
- moved U4 165.7 mm to (150.4, 148.6)
- moved C8 164.3 mm to (138.7, 54.1)
- moved U2 162.8 mm to (150.4, 55.1), turned to 0 degrees
- moved F1 161.8 mm to (135.4, 54.1), turned to 0 degrees
- moved D6 153.4 mm to (172.2, 65.0)
- moved R19 152.0 mm to (167.9, 114.8), turned to 0 degrees
- moved D3 151.2 mm to (167.9, 116.8), turned to 0 degrees
- moved D7 150.2 mm to (165.4, 97.3)
- moved F7 150.2 mm to (164.8, 110.5), turned to 0 degrees
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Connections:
- R56 pad 1: VCHRG -> Net-(U8-SENSE)
- R57 pad 1: GND -> /Solar Charger/A0_S
- R57 pad 2: Net-(U8-A0) -> MAIN_3V3
- U1 pad 1: Net-(J1-Pin_1) -> /Interfaces/D_CONN+
- U1 pad 2: GND -> GNDREF
- U1 pad 3: Net-(J1-Pin_2) -> /Interfaces/D_CONN-
- U1 pad 4: SDA -> /Interfaces/D-
- U1 pad 5: MAIN_3V3 -> USB_5V
- U1 pad 6: SCL -> /Interfaces/D+
- U8 pad 1: VBATT -> Net-(U8-VCC)
- U8 pad 2: VCHRG -> Net-(U8-SENSE)
- U8 pad 8: Net-(U8-A0) -> /Solar Charger/A0_S
- U8 pad 9: unconnected-(U8-A1-Pad9) -> /Solar Charger/A1_S
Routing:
- net GND: track 0.00 -> 33.2 mm, vias 0 -> 13
- net SCL: track 0.00 -> 26.6 mm
- net /Sun Pyramid/LS2_SCL: track 0.00 -> 23.0 mm
- net SDA: track 0.00 -> 22.8 mm
- net Net-(Q20A-D1): track 0.00 -> 19.9 mm
- net /Sun Pyramid/LS0_SDA: track 0.00 -> 12.9 mm
- net /Coil Driver/SDA_M: track 2.01 -> 14.8 mm
- net /Sun Pyramid/LS3_SDA: track 0.00 -> 12.8 mm
- net /Sun Pyramid/LS3_SCL: track 0.00 -> 12.8 mm
- net /Sun Pyramid/LS1_SCL: track 0.00 -> 12.8 mm
- net /Sun Pyramid/LS1_SDA: track 0.00 -> 12.8 mm
- net /Coil Driver/SCL_M: track 2.02 -> 14.9 mm
- net /Sun Pyramid/LS0_SCL: track 0.00 -> 12.8 mm
- net /Sun Pyramid/LS2_SDA: track 0.00 -> 12.8 mm
- net USB_5V: track 0.00 -> 12.8 mm
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- added copper zone on F.Cu, net GNDREF

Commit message: Uncommitted changes
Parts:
- moved F7 1.57 mm to (163.3, 110.1)
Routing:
- net /Solar Charger/MPPT2/VCC: track 0.00 -> 12.4 mm
- net GND: track 33.2 -> 38.8 mm
- net Net-(U9-MODE): track 0.00 -> 5.31 mm
- net /Solar Charger/MPPT2/MPPC: track 0.00 -> 5.01 mm
- net Net-(U9-EXTVCC): track 0.00 -> 4.32 mm
- net /Solar Charger/PGOOD3: track 0.00 -> 3.80 mm
- net /Solar Charger/MPPT2/RUN: track 0.00 -> 3.67 mm
- net Net-(U9-ILIM): track 0.00 -> 3.28 mm
- net /Solar Charger/MPPT2/FB: track 0.00 -> 3.28 mm
- net /Solar Charger/Charge OR-ing2/IN: vias 0 -> 1
- added copper zone on B.Cu, net (none)
- added copper zone on B.Cu, net /Solar Charger/Charge OR-ing2/IN
- added copper zone on B.Cu, net /Solar Charger/MPPT2/VIN
- added copper zone on B.Cu, net Net-(U9-BST1)
- added copper zone on B.Cu, net Net-(U9-SW1)
- added copper zone on B.Cu, net Net-(U9-SW2)
- removed copper zone on B.Cu, net GND
- removed copper zone on F.Cu, net GND

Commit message: More layout work
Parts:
- moved D5 34.5 mm to (162.8, 65.0)
- moved R16 13.2 mm to (122.7, 95.8), turned to 0 degrees
- moved R77 13.2 mm to (127.8, 108.0), turned to 180 degrees
- moved R101 13.2 mm to (172.5, 95.8), turned to 0 degrees
- moved R95 13.2 mm to (177.5, 108.0), turned to 180 degrees
- moved C29 12.5 mm to (128.5, 96.5), turned to 90 degrees
- moved C9 12.5 mm to (121.9, 107.2), turned to -90 degrees
- moved C32 12.5 mm to (178.3, 96.5), turned to 90 degrees
- moved C33 12.5 mm to (171.7, 107.2), turned to -90 degrees
- moved R18 11.2 mm to (123.4, 107.2), turned to 90 degrees
- moved R79 11.2 mm to (127.0, 96.5), turned to -90 degrees
- moved R103 11.2 mm to (173.2, 107.2), turned to 90 degrees
- moved R97 11.2 mm to (176.8, 96.5), turned to -90 degrees
- moved R14 10.7 mm to (125.2, 107.2), turned to 90 degrees
- moved R75 10.7 mm to (125.2, 96.5), turned to -90 degrees
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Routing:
- net GNDREF: track 0.00 -> 92.1 mm, vias 0 -> 2
- net /Sun Pyramid/LS0_3V3: track 0.00 -> 85.9 mm, vias 0 -> 3
- net Net-(D6-K): track 0.00 -> 72.0 mm, vias 0 -> 2
- net Net-(D8-K): track 0.00 -> 69.9 mm, vias 0 -> 2
- net /Sun Pyramid/LS2_3V3: track 0.00 -> 68.6 mm, vias 0 -> 3
- net /Sun Pyramid/LS1_3V3: track 0.00 -> 62.3 mm, vias 0 -> 3
- net /Sun Pyramid/LS2_SCL: track 23.0 -> 70.0 mm, vias 0 -> 1
- net /Sun Pyramid/LS0_SDA: track 12.9 -> 58.1 mm, vias 0 -> 1
- net USB_5V: track 12.8 -> 57.4 mm, vias 0 -> 1
- net /Interfaces/D_CONN-: track 0.00 -> 44.5 mm, vias 0 -> 1
- net /Interfaces/D_CONN+: track 0.00 -> 43.7 mm, vias 0 -> 1
- net /Sun Pyramid/LS0_SCL: track 12.8 -> 52.3 mm, vias 0 -> 1
- net Net-(D10-A): track 0.00 -> 34.2 mm
- net Net-(D5-K): track 0.00 -> 33.9 mm
- net Net-(D7-K): track 0.00 -> 30.5 mm, vias 0 -> 4
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- added copper zone on B.Cu, net GND
- added copper zone on F.Cu, net GND
- added copper zone on B.Cu, net Net-(D2-A)
- added copper zone on B.Cu, net Net-(D6-K)
- added copper zone on F.Cu, net Net-(D6-K)
- added copper zone on B.Cu, net Net-(D7-K)
- added copper zone on F.Cu, net Net-(D7-K)
- added copper zone on B.Cu, net Net-(D8-K)
- added copper zone on F.Cu, net Net-(D8-K)
- added copper zone on B.Cu, net Net-(Q9-S)
- added copper zone on B.Cu, net Net-(U9-BST2)
- added copper zone on B.Cu, net VCHRG
- removed copper zone on B.Cu, net (none)
